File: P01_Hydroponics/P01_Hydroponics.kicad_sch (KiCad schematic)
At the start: 0 parts

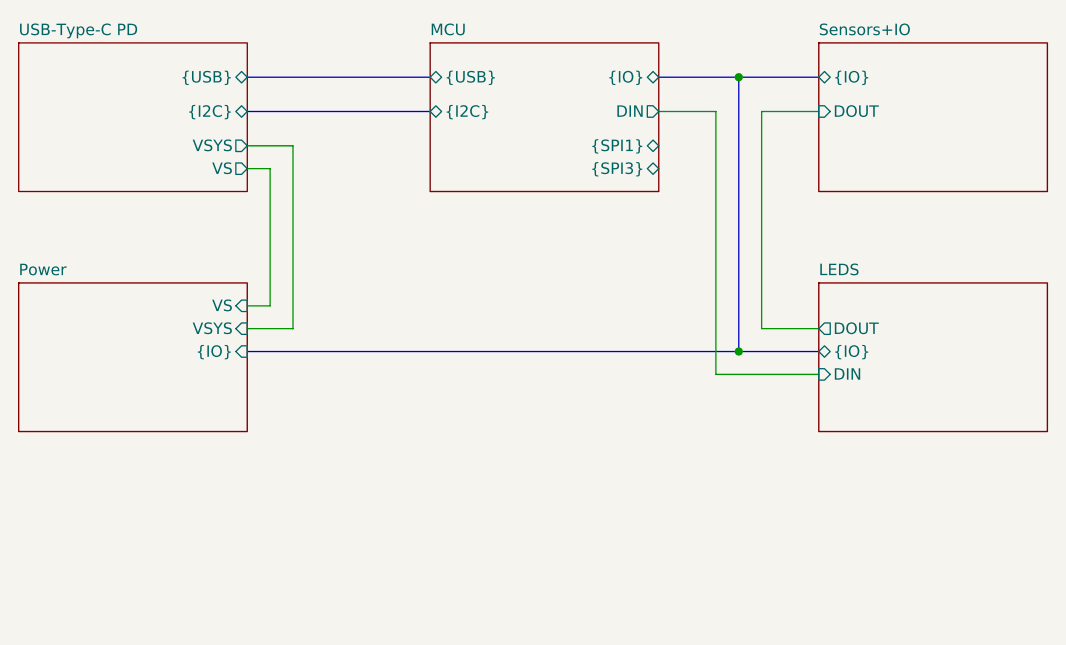
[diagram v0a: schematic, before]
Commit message: Need review
Updated:
STD14 to tag connect.
Added most footprints.
Change crystal to oscillator for ESP32
Rearrange radio controller schematic.
Added NOR flash.
Added USB-C connector for ESP32
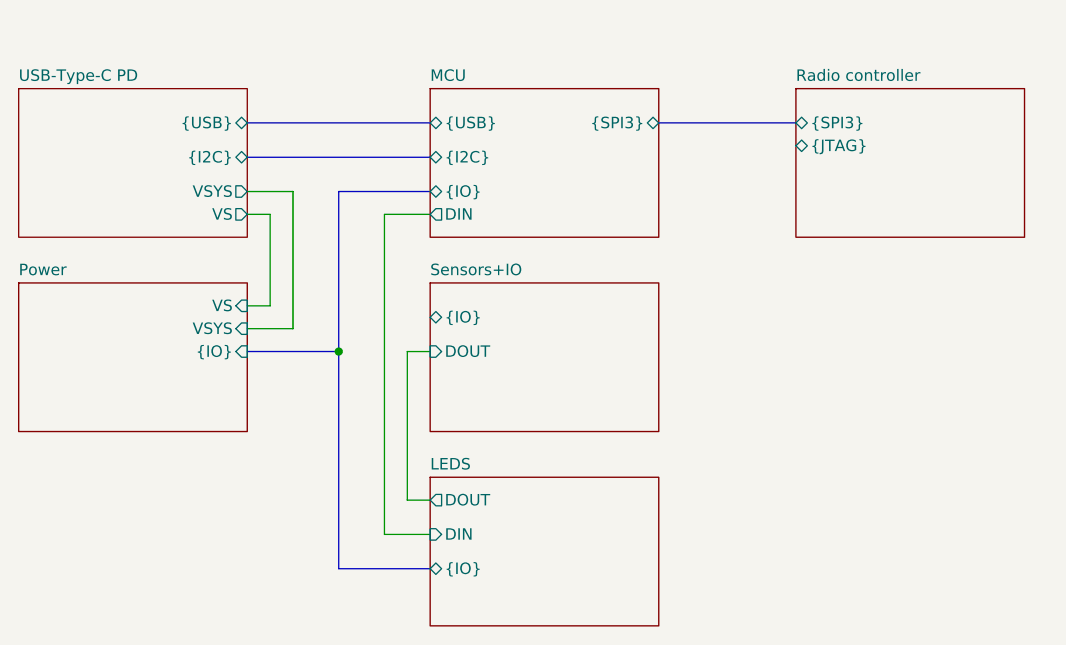
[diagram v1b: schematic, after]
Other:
- added sheet Radio controller (Radio controller.kicad_sch)
- sheet MCU ports: added none; removed {SPI1}
